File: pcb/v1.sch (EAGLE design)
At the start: 49 parts, among them U2 MMBT3904, U3 MMBT3904, U4 MMBT3904, U5 MMBT3904

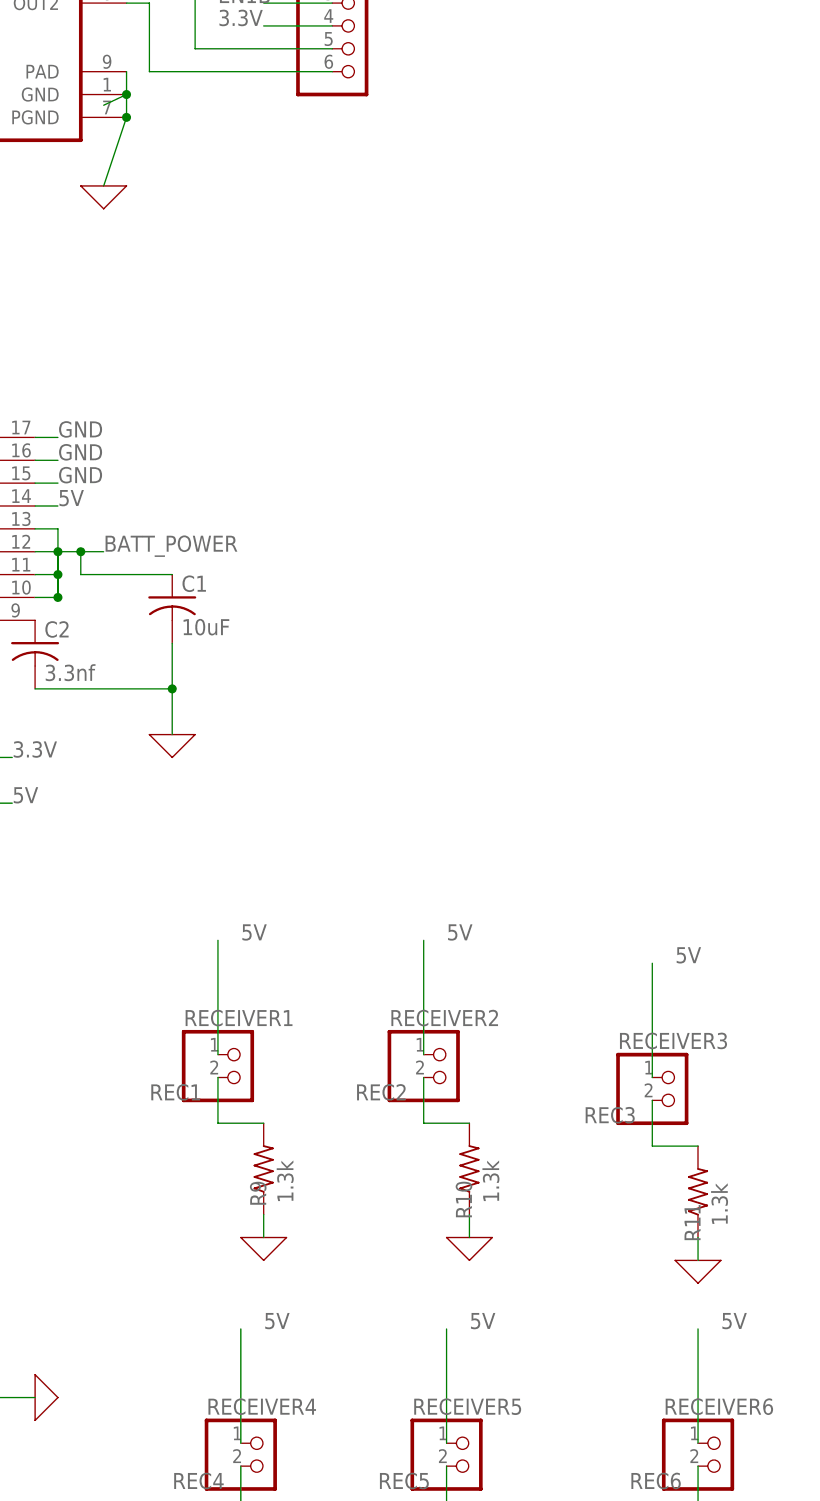
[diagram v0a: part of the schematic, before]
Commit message: Changed 5V receiver inputs to 3.3V
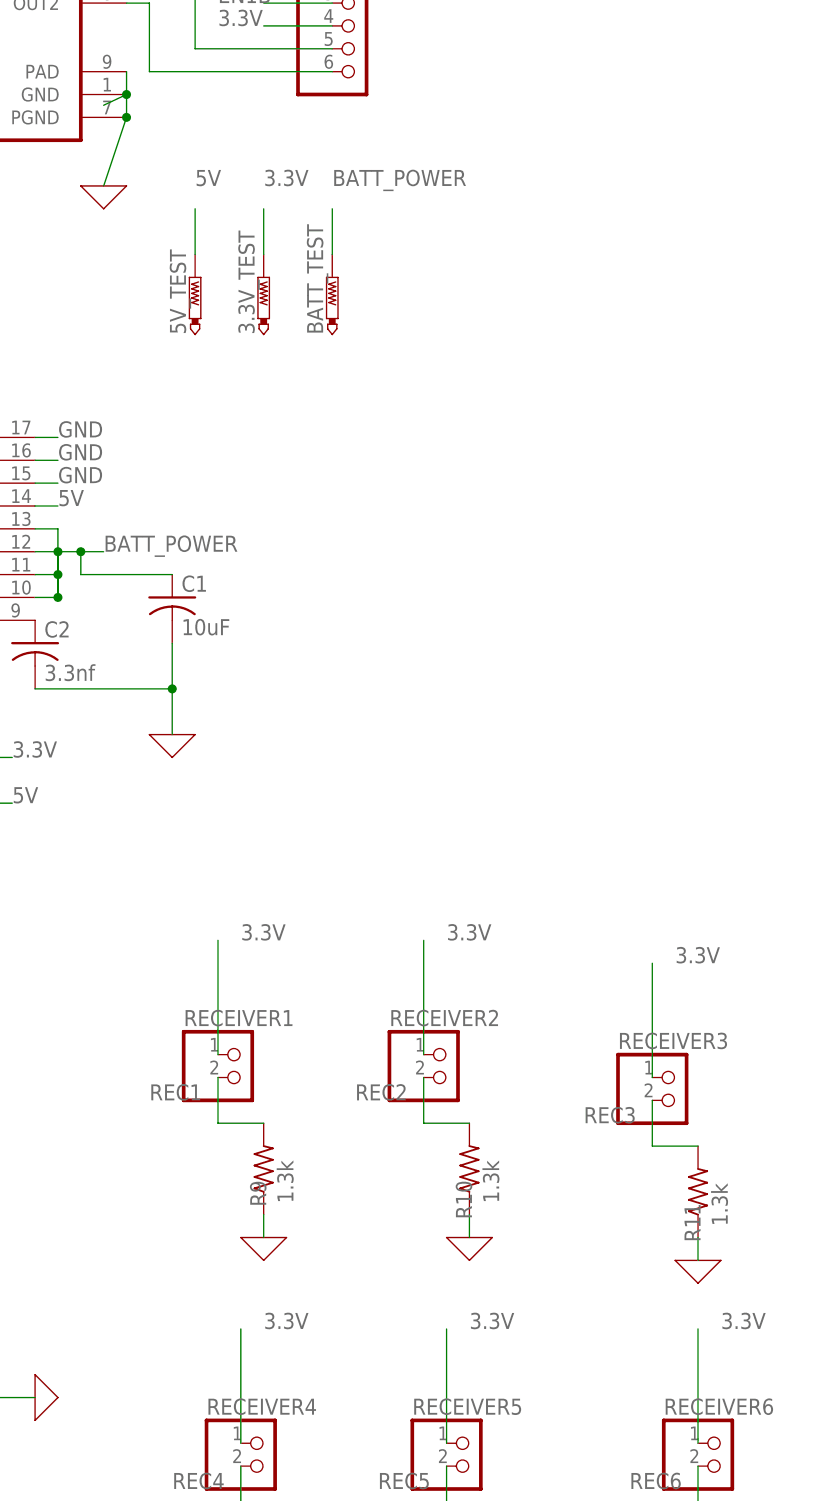
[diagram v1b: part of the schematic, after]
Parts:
- added 3.3V_TEST, 5V_TEST, BATT_TEST: PTR1B1,27, testpad:PTR1B1,27
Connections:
- net 3.3V: now also 3.3V_TEST.TP, RECEIVER1.1, RECEIVER2.1, RECEIVER3.1, RECEIVER4.1, RECEIVER5.1, RECEIVER6.1
- net 5V: now also 5V_TEST.TP; no longer RECEIVER1.1, RECEIVER2.1, RECEIVER3.1, RECEIVER4.1, RECEIVER5.1, RECEIVER6.1
- net BATT_POWER: now also BATT_TEST.TP
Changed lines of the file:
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@@
 <part name="C8" library="rcl" library_urn="urn:adsk.eagle:library:334" deviceset="C-US" device="C0805" package3d_urn="urn:adsk.eagle:package:23617/2" value="22uF"/>
 <part name="L1" library="XFL4020" deviceset="XFL4020" device="" value="2.2uH"/>
+<part name="5V_TEST" library="testpad" library_urn="urn:adsk.eagle:library:385" deviceset="PTR1" device="B1,27" package3d_urn="urn:adsk.eagle:package:27944/1"/>
+<part name="3.3V_TEST" library="testpad" library_urn="urn:adsk.eagle:library:385" deviceset="PTR1" device="B1,27" package3d_urn="urn:adsk.eagle:package:27944/1"/>
+<part name="BATT_TEST" library="testpad" library_urn="urn:adsk.eagle:library:385" deviceset="PTR1" device="B1,27" package3d_urn="urn:adsk.eagle:package:27944/1"/>
 </parts>
 <sheets>
@@
 <attribute name="VALUE" x="48.26" y="128.27" size="1.778" layer="96" rot="R180"/>
 </instance>
+<instance part="5V_TEST" gate="G$1" x="129.54" y="142.24" smashed="yes">
+<attribute name="NAME" x="128.524" y="135.89" size="1.778" layer="95" rot="R90"/>
+<attribute name="TP_SIGNAL_NAME" x="130.81" y="139.7" size="1.778" layer="97"/>
+</instance>
+<instance part="3.3V_TEST" gate="G$1" x="137.16" y="142.24" smashed="yes">
+<attribute name="NAME" x="136.144" y="135.89" size="1.778" layer="95" rot="R90"/>
+<attribute name="TP_SIGNAL_NAME" x="138.43" y="139.7" size="1.778" layer="97"/>
+</instance>
+<instance part="BATT_TEST" gate="G$1" x="144.78" y="142.24" smashed="yes">
+<attribute name="NAME" x="143.764" y="135.89" size="1.778" layer="95" rot="R90"/>
+<attribute name="TP_SIGNAL_NAME" x="146.05" y="139.7" size="1.778" layer="97"/>
+</instance>
 </instances>
 <busses>
@@
 <label x="132.08" y="170.18" size="1.778" layer="95"/>
 </segment>
+<segment>
+<pinref part="3.3V_TEST" gate="G$1" pin="TP"/>
+<wire x1="137.16" y1="144.78" x2="137.16" y2="149.86" width="0.1524" layer="91"/>
+<label x="137.16" y="152.4" size="1.778" layer="95"/>
+</segment>
+<segment>
+<pinref part="RECEIVER1" gate="G$1" pin="1"/>
+<label x="134.62" y="68.58" size="1.778" layer="95"/>
+<wire x1="132.08" y1="55.88" x2="132.08" y2="68.58" width="0.1524" layer="91"/>
+</segment>
+<segment>
+<pinref part="RECEIVER2" gate="G$1" pin="1"/>
+<label x="157.48" y="68.58" size="1.778" layer="95"/>
+<wire x1="154.94" y1="55.88" x2="154.94" y2="68.58" width="0.1524" layer="91"/>
+</segment>
+<segment>
+<pinref part="RECEIVER3" gate="G$1" pin="1"/>
+<label x="182.88" y="66.04" size="1.778" layer="95"/>
+<wire x1="180.34" y1="53.34" x2="180.34" y2="66.04" width="0.1524" layer="91"/>
+</segment>
+<segment>
+<pinref part="RECEIVER4" gate="G$1" pin="1"/>
+<label x="137.16" y="25.4" size="1.778" layer="95"/>
+<wire x1="134.62" y1="12.7" x2="134.62" y2="25.4" width="0.1524" layer="91"/>
+</segment>
+<segment>
+<pinref part="RECEIVER5" gate="G$1" pin="1"/>
+<label x="160.02" y="25.4" size="1.778" layer="95"/>
+<wire x1="157.48" y1="12.7" x2="157.48" y2="25.4" width="0.1524" layer="91"/>
+</segment>
+<segment>
+<pinref part="RECEIVER6" gate="G$1" pin="1"/>
+<label x="187.96" y="25.4" size="1.778" layer="95"/>
+<wire x1="185.42" y1="12.7" x2="185.42" y2="25.4" width="0.1524" layer="91"/>
+</segment>
 </net>
 <net name="5V" class="0">
@@
 <label x="2.54" y="104.14" size="1.778" layer="95"/>
 <pinref part="LED1" gate="G$1" pin="A"/>
-</segment>
-<segment>
-<pinref part="RECEIVER1" gate="G$1" pin="1"/>
-<label x="134.62" y="68.58" size="1.778" layer="95"/>
-<wire x1="132.08" y1="55.88" x2="132.08" y2="68.58" width="0.1524" layer="91"/>
-</segment>
-<segment>
-<pinref part="RECEIVER2" gate="G$1" pin="1"/>
-<label x="157.48" y="68.58" size="1.778" layer="95"/>
-<wire x1="154.94" y1="55.88" x2="154.94" y2="68.58" width="0.1524" layer="91"/>
-</segment>
-<segment>
-<pinref part="RECEIVER3" gate="G$1" pin="1"/>
-<label x="182.88" y="66.04" size="1.778" layer="95"/>
-<wire x1="180.34" y1="53.34" x2="180.34" y2="66.04" width="0.1524" layer="91"/>
-</segment>
-<segment>
-<pinref part="RECEIVER4" gate="G$1" pin="1"/>
-<label x="137.16" y="25.4" size="1.778" layer="95"/>
-<wire x1="134.62" y1="12.7" x2="134.62" y2="25.4" width="0.1524" layer="91"/>
-</segment>
-<segment>
-<pinref part="RECEIVER5" gate="G$1" pin="1"/>
-<label x="160.02" y="25.4" size="1.778" layer="95"/>
-<wire x1="157.48" y1="12.7" x2="157.48" y2="25.4" width="0.1524" layer="91"/>
-</segment>
-<segment>
-<pinref part="RECEIVER6" gate="G$1" pin="1"/>
-<label x="187.96" y="25.4" size="1.778" layer="95"/>
-<wire x1="185.42" y1="12.7" x2="185.42" y2="25.4" width="0.1524" layer="91"/>
 </segment>
 <segment>
@@
 <label x="7.62" y="48.26" size="1.778" layer="95"/>
 <pinref part="LED4" gate="G$1" pin="A"/>
+</segment>
+<segment>
+<pinref part="5V_TEST" gate="G$1" pin="TP"/>
+<wire x1="129.54" y1="144.78" x2="129.54" y2="149.86" width="0.1524" layer="91"/>
+<label x="129.54" y="152.4" size="1.778" layer="95"/>
 </segment>
 </net>
@@
 <label x="109.22" y="185.42" size="1.778" layer="95"/>
 </segment>
-</net>
+<segment>
+<pinref part="BATT_TEST" gate="G$1" pin="TP"/>
+<wire x1="144.78" y1="144.78" x2="144.78" y2="149.86" width="0.1524" layer="91"/>
+<label x="144.78" y="152.4" size="1.778" layer="95"/>
+</segment>
+</net>

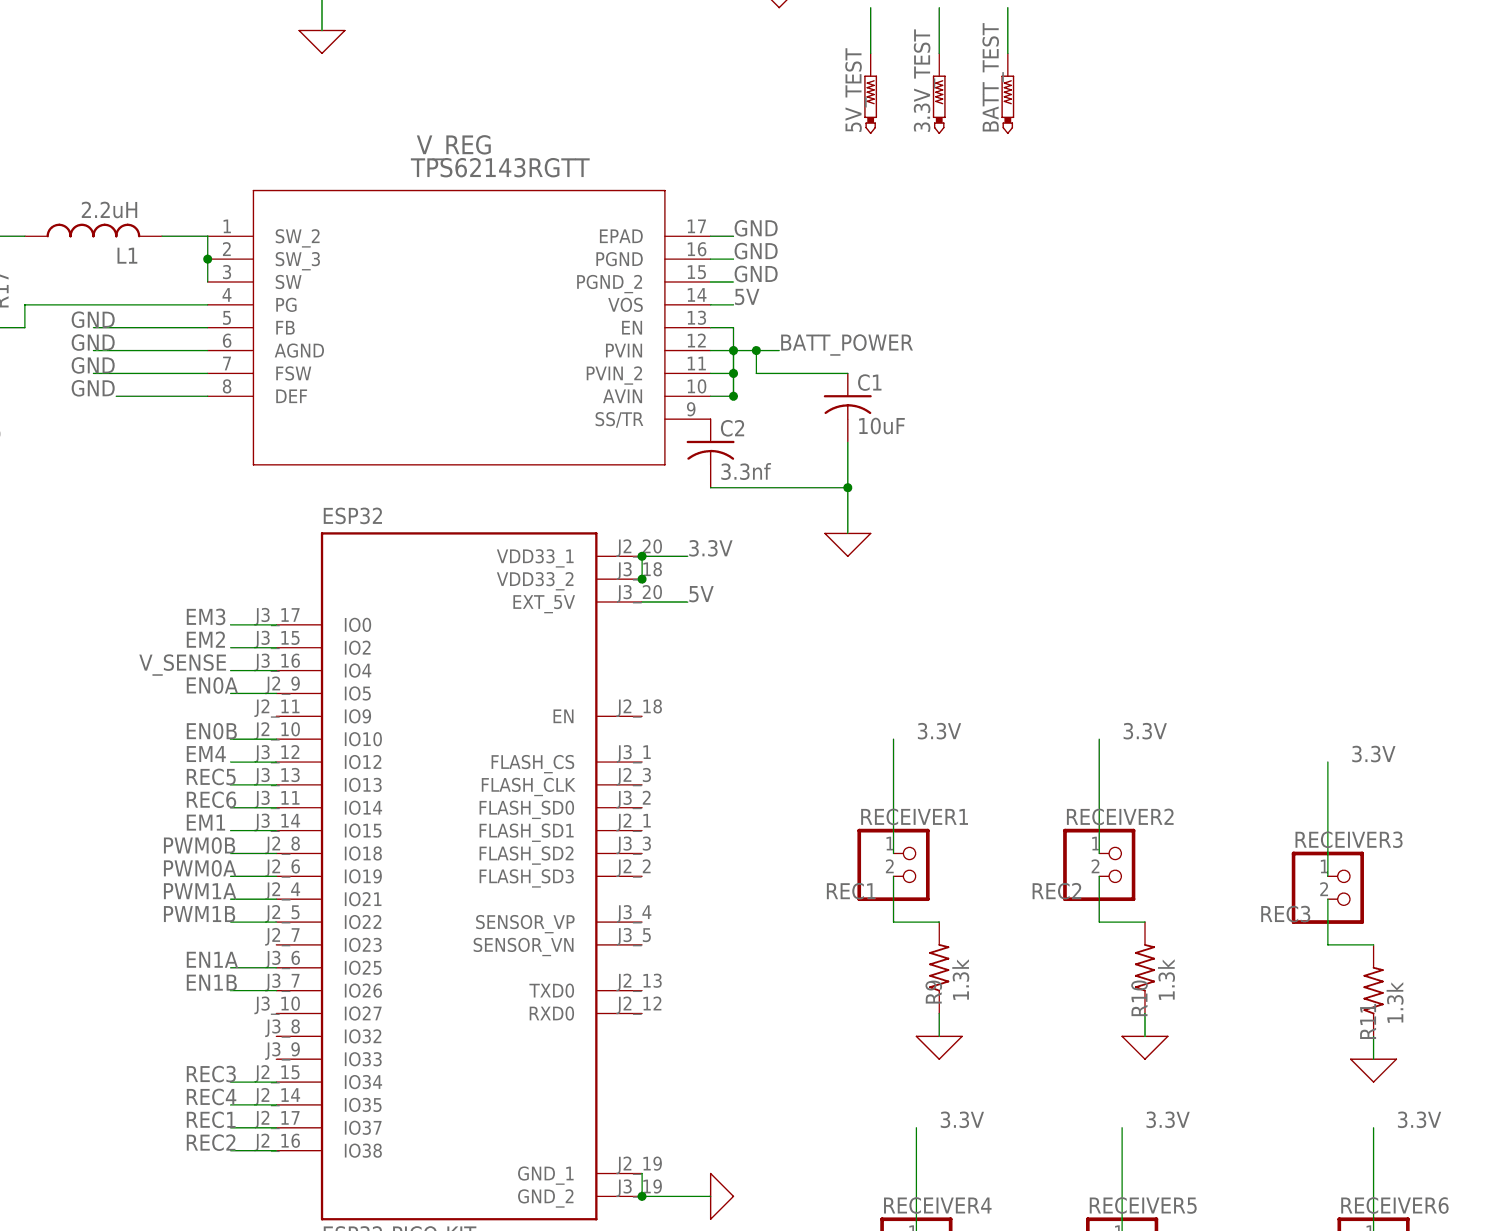
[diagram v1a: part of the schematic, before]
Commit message: Added Smd led
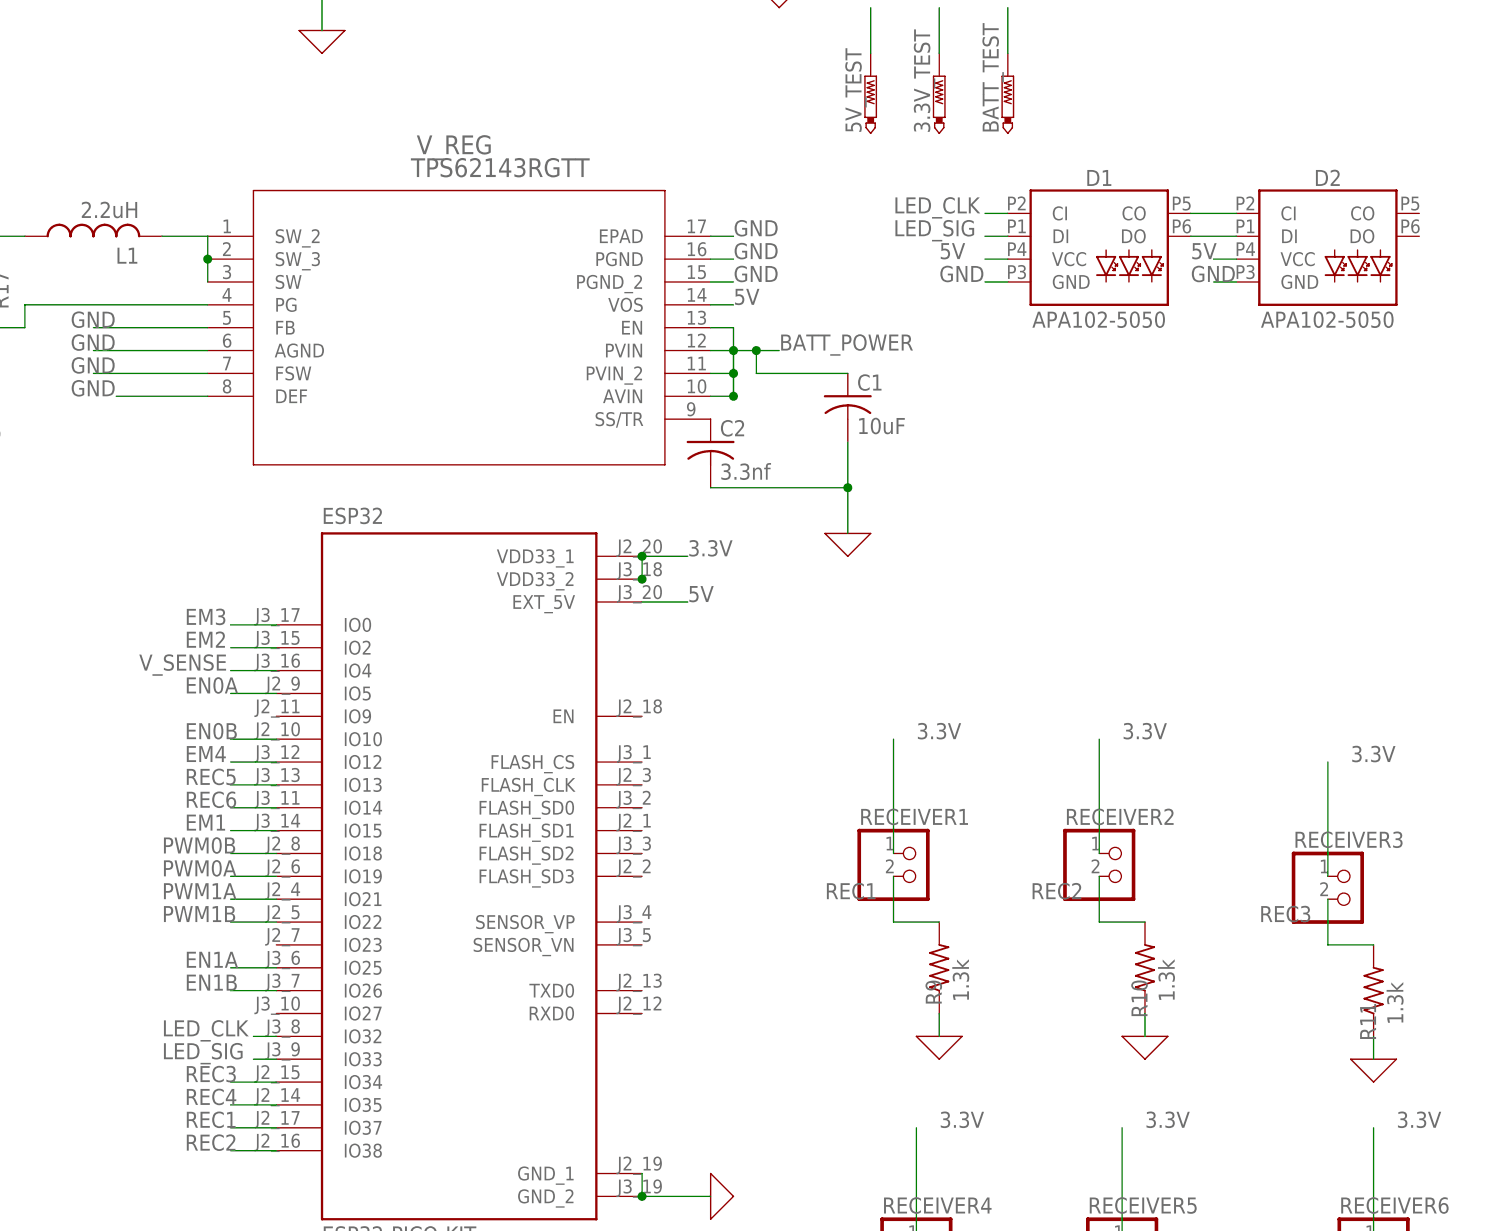
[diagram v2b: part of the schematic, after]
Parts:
- added D1, D2: APA102-5050, SparkFun-LED:APA102-5050
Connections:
- new net LED_CLK: D1.CI, ESP32.IO32
- new net LED_SIG: D1.DI, ESP32.IO33
- new net N$34: D1.CO, D2.CI
- new net N$35: D1.DO, D2.DI
- net 5V: now also D1.VCC, D2.VCC
- net GND: now also D1.GND, D2.GND
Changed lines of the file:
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@@
 <part name="3.3V_TEST" library="testpad" library_urn="urn:adsk.eagle:library:385" deviceset="PTR1" device="B1,27" package3d_urn="urn:adsk.eagle:package:27944/1"/>
 <part name="BATT_TEST" library="testpad" library_urn="urn:adsk.eagle:library:385" deviceset="PTR1" device="B1,27" package3d_urn="urn:adsk.eagle:package:27944/1"/>
+<part name="D1" library="SparkFun-LED" deviceset="APA102" device="-5050"/>
+<part name="D2" library="SparkFun-LED" deviceset="APA102" device="-5050"/>
 </parts>
 <sheets>
@@
 <attribute name="TP_SIGNAL_NAME" x="146.05" y="139.7" size="1.778" layer="97"/>
 </instance>
+<instance part="D1" gate="G$1" x="154.94" y="124.46" smashed="yes">
+<attribute name="NAME" x="154.94" y="130.048" size="1.778" layer="95" font="vector" align="bottom-center"/>
+<attribute name="VALUE" x="154.94" y="114.3" size="1.778" layer="96" font="vector" align="bottom-center"/>
+</instance>
+<instance part="D2" gate="G$1" x="180.34" y="124.46" smashed="yes">
+<attribute name="NAME" x="180.34" y="130.048" size="1.778" layer="95" font="vector" align="bottom-center"/>
+<attribute name="VALUE" x="180.34" y="114.3" size="1.778" layer="96" font="vector" align="bottom-center"/>
+</instance>
 </instances>
 <busses>
@@
 <wire x1="129.54" y1="144.78" x2="129.54" y2="149.86" width="0.1524" layer="91"/>
 <label x="129.54" y="152.4" size="1.778" layer="95"/>
+</segment>
+<segment>
+<pinref part="D1" gate="G$1" pin="VCC"/>
+<wire x1="144.78" y1="121.92" x2="142.24" y2="121.92" width="0.1524" layer="91"/>
+<label x="137.16" y="121.92" size="1.778" layer="95"/>
+</segment>
+<segment>
+<pinref part="D2" gate="G$1" pin="VCC"/>
+<wire x1="170.18" y1="121.92" x2="167.64" y2="121.92" width="0.1524" layer="91"/>
+<label x="165.1" y="121.92" size="1.778" layer="95"/>
 </segment>
 </net>
@@
 <label x="-38.1" y="7.62" size="1.778" layer="95"/>
 </segment>
+<segment>
+<pinref part="D1" gate="G$1" pin="GND"/>
+<wire x1="144.78" y1="119.38" x2="142.24" y2="119.38" width="0.1524" layer="91"/>
+<label x="137.16" y="119.38" size="1.778" layer="95"/>
+</segment>
+<segment>
+<pinref part="D2" gate="G$1" pin="GND"/>
+<wire x1="170.18" y1="119.38" x2="167.64" y2="119.38" width="0.1524" layer="91"/>
+<label x="165.1" y="119.38" size="1.778" layer="95"/>
+</segment>
 </net>
 <net name="N$2" class="0">
@@
 </segment>
 </net>
+<net name="LED_CLK" class="0">
+<segment>
+<pinref part="ESP32" gate="G$1" pin="IO32"/>
+<wire x1="63.5" y1="35.56" x2="60.96" y2="35.56" width="0.1524" layer="91"/>
+<label x="50.8" y="35.56" size="1.778" layer="95"/>
+</segment>
+<segment>
+<pinref part="D1" gate="G$1" pin="CI"/>
+<wire x1="144.78" y1="127" x2="142.24" y2="127" width="0.1524" layer="91"/>
+<label x="132.08" y="127" size="1.778" layer="95"/>
+</segment>
+</net>
+<net name="LED_SIG" class="0">
+<segment>
+<pinref part="ESP32" gate="G$1" pin="IO33"/>
+<wire x1="63.5" y1="33.02" x2="60.96" y2="33.02" width="0.1524" layer="91"/>
+<label x="50.8" y="33.02" size="1.778" layer="95"/>
+</segment>
+<segment>
+<pinref part="D1" gate="G$1" pin="DI"/>
+<wire x1="144.78" y1="124.46" x2="142.24" y2="124.46" width="0.1524" layer="91"/>
+<label x="132.08" y="124.46" size="1.778" layer="95"/>
+</segment>
+</net>
+<net name="N$34" class="0">
+<segment>
+<pinref part="D1" gate="G$1" pin="CO"/>
+<pinref part="D2" gate="G$1" pin="CI"/>
+<wire x1="165.1" y1="127" x2="170.18" y2="127" width="0.1524" layer="91"/>
+</segment>
+</net>
+<net name="N$35" class="0">
+<segment>
+<pinref part="D1" gate="G$1" pin="DO"/>
+<pinref part="D2" gate="G$1" pin="DI"/>
+<wire x1="165.1" y1="124.46" x2="170.18" y2="124.46" width="0.1524" layer="91"/>
+</segment>
+</net>
